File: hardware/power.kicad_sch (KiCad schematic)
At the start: 10 parts, among them J1 Conn_01x02_Pin, U2 TPS7A91

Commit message: feat(kicad): Added several open sourced footprint libraries, finished schematic design for nrf, uwb, tof, flash, motors and added all reference material to refs folder
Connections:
- net BAT_SENS renamed BAT_SENSE
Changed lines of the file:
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@@
 		)
 	)
-	(hierarchical_label "BAT_SENS"
+	(hierarchical_label "BAT_SENSE"
 		(shape output)
 		(at 57.15 57.15 0)

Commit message: feat(kicad): Cleared ERC errors and assigned footprints for all parts
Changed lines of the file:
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@@
+	)
+	(junction
+		(at 34.29 29.21)
+		(diameter 0)
+		(color 0 0 0 0)
 	)
 	(junction
@@
 			(width 0)
 			(type default)
-		)
-	)
-	(label ""
-		(at 43.18 57.15 0)
-		(effects
-			(font
-				(size 1.27 1.27)
-			)
-			(justify left bottom)
 		)
 	)
@@
 					(unit 1)
 				)
+			)
+		)
+	)
+	(symbol
+		(lib_id "power:PWR_FLAG")
+		(at 34.29 29.21 90)
+		(unit 1)
+		(body_style 1)
+		(exclude_from_sim no)
+		(in_bom yes)
+		(on_board yes)
+		(in_pos_files yes)
+		(dnp no)
+		(fields_autoplaced yes)
+		(property "Reference" "#FLG01"
+			(at 32.385 29.21 0)
+			(hide yes)
+			(show_name no)
+			(do_not_autoplace no)
+			(effects
+				(font
+					(size 1.27 1.27)
+				)
+			)
+		)
+		(property "Value" "PWR_FLAG"
+			(at 30.48 29.2099 90)
+			(show_name no)
+			(do_not_autoplace no)
+			(effects
+				(font
+					(size 1.27 1.27)
+				)
+				(justify left)
+			)
+		)
+		(property "Footprint" ""
+			(at 34.29 29.21 0)
+			(hide yes)
+			(show_name no)
+			(do_not_autoplace no)
+			(effects
+				(font
+					(size 1.27 1.27)
+				)
+			)
+		)
+		(property "Datasheet" ""
+			(at 34.29 29.21 0)
+			(hide yes)
+			(show_name no)
+			(do_not_autoplace no)
+			(effects
+				(font
+					(size 1.27 1.27)
+				)
+			)
+		)
+		(property "Description" "Special symbol for telling ERC where power comes from"
+			(at 34.29 29.21 0)
+			(hide yes)
+			(show_name no)
+			(do_not_autoplace no)
+			(effects
+				(font
+					(size 1.27 1.27)
+				)
+			)
+		)
+		(pin "1"
+		)
+		(instances
+			(project "swarm_drone"
+				(path "/3a60ba80-6c79-4a64-bdfd-12960f1d2492/44f345a2-ae6d-4d47-8f7c-a9b5694879b4"
+					(reference "#FLG01")
+					(unit 1)
+				)

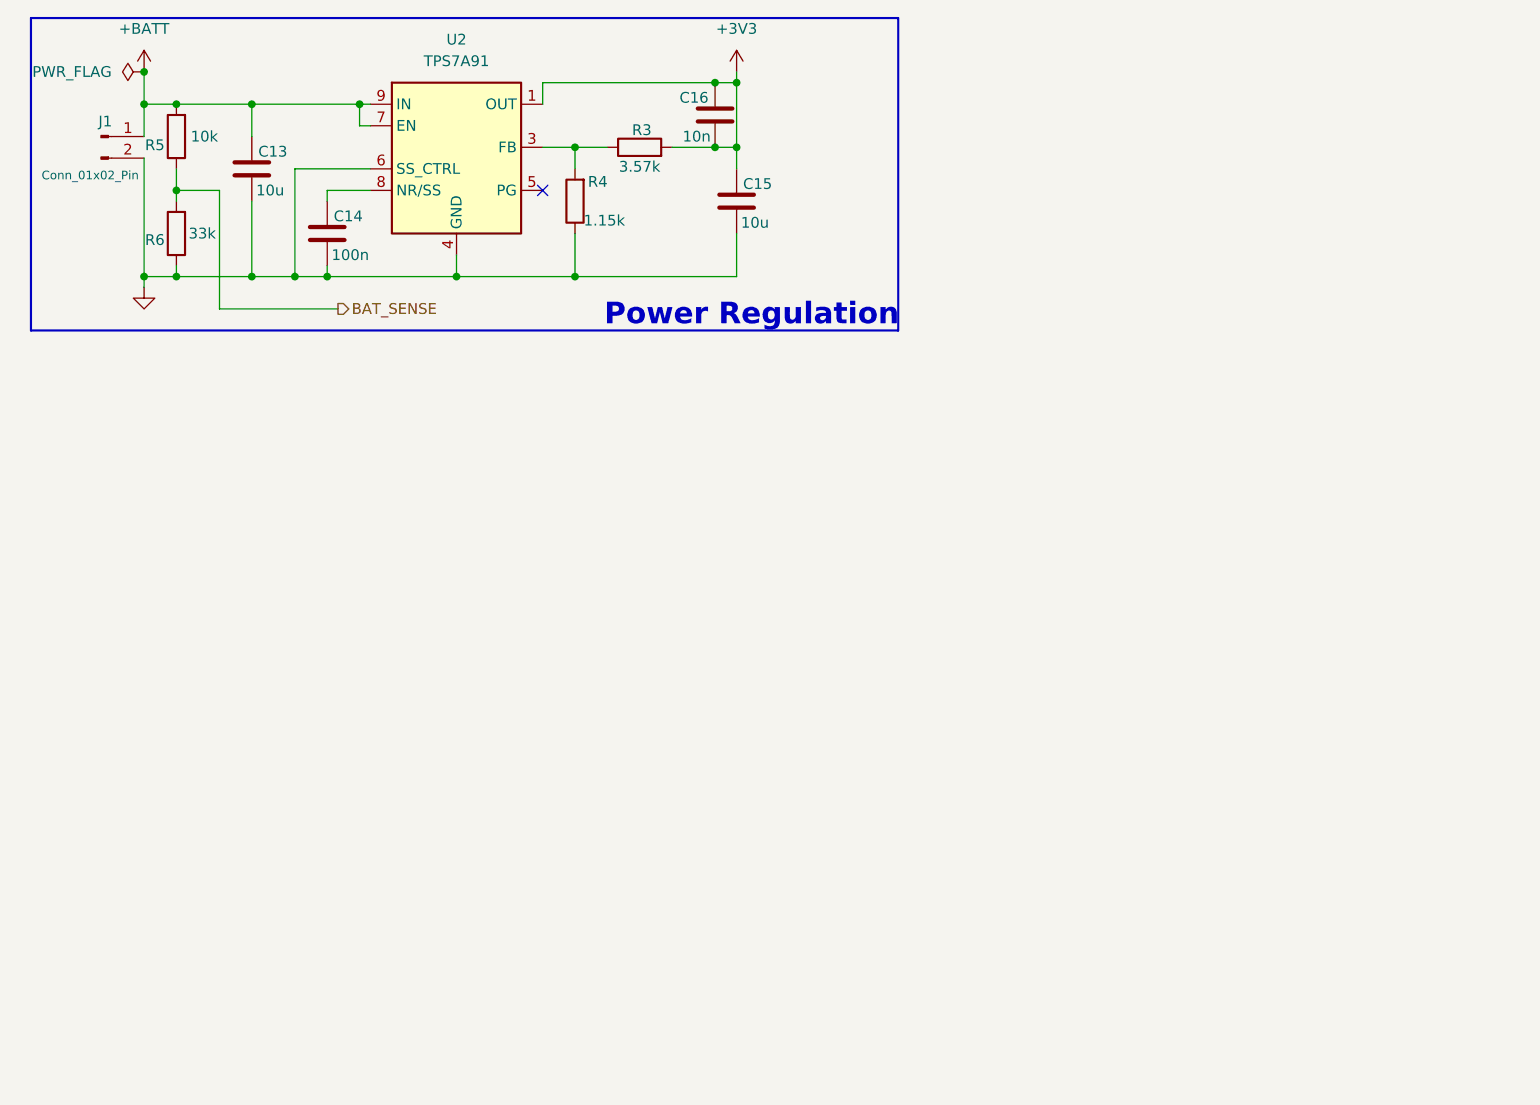
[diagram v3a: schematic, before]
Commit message: feat(kicad): Added Application notes for the LDO
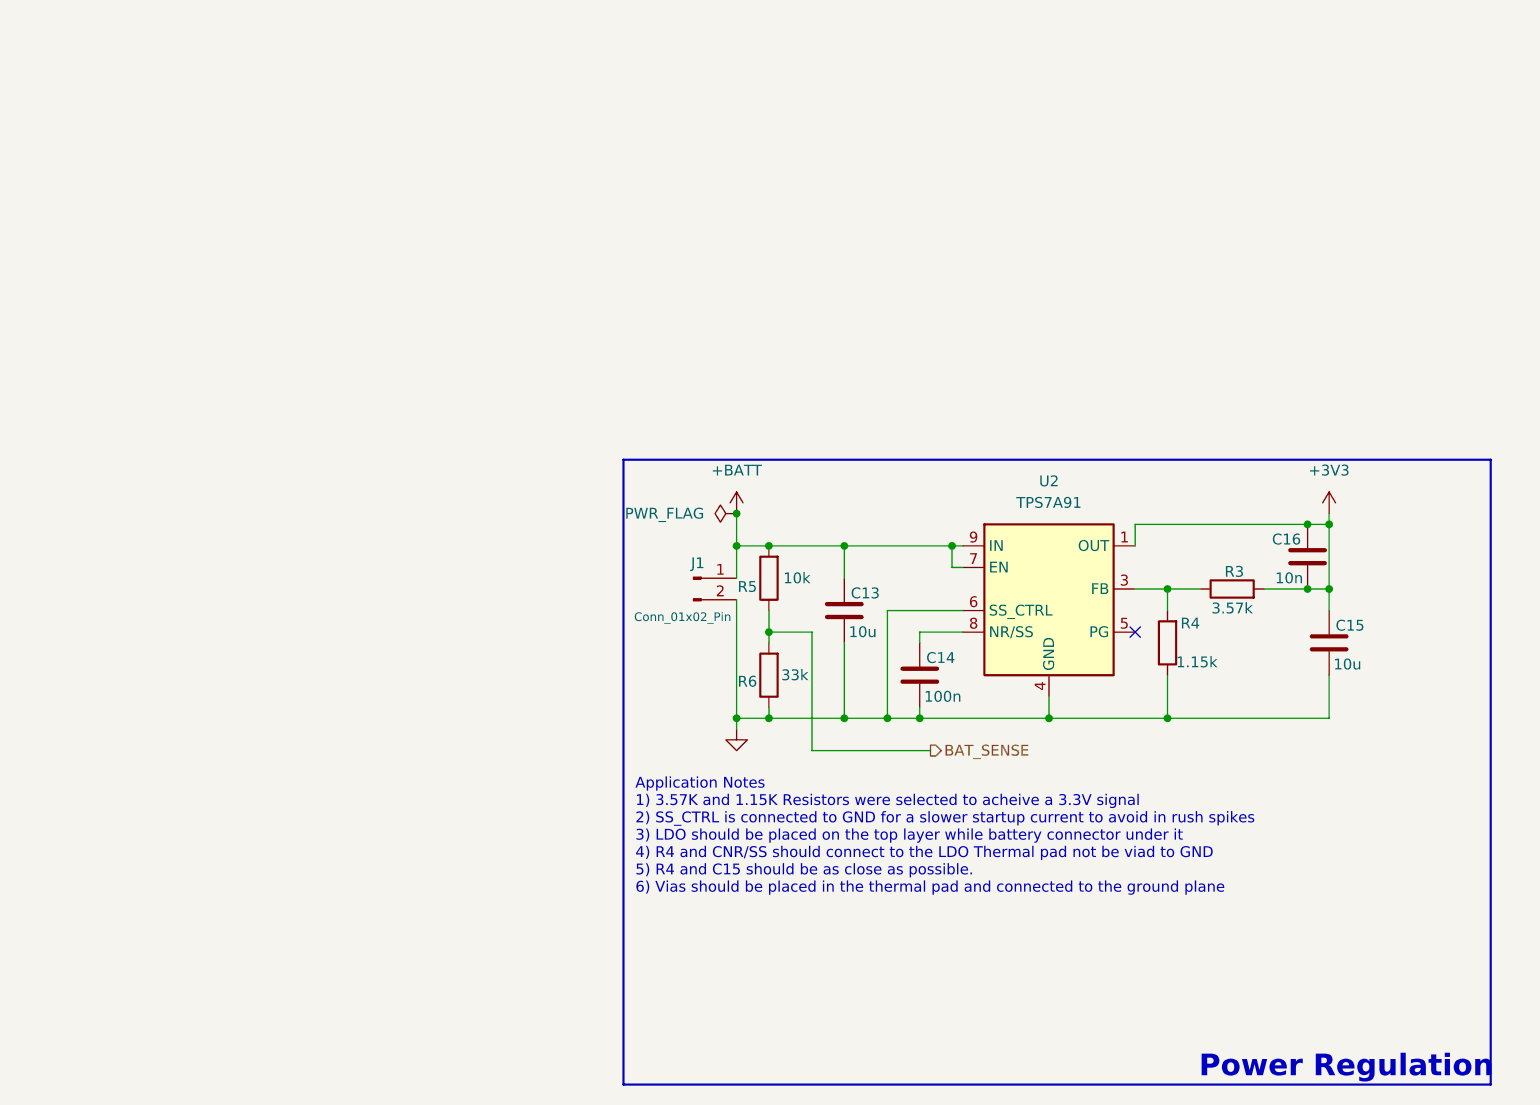
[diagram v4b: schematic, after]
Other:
- note added: "Application Notes 1) 3.57K and 1.15K Resistors were selected to acheive a 3.3V signal 2) SS_CTRL is connected to GND for a slower startup current to avoid in rush spikes 3) LDO should be placed on the top layer while battery connector under it 4) R4 and CNR/SS should connect to the LDO Thermal pad not be viad to GND 5) R4 and C15 should be as close as possible. 6) Vias should be placed in the the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"
- moved on the sheet: C13, C14, C15, C16, J1, R3, R4, R5, R6, U2
